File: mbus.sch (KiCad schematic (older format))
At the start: 17 parts, among them Q1 PN2222A, Q2 PN2222A, Q3 BC640, Q4 PN2222A

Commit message: some cosmetics and comments
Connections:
- net GND: now also R5.2; no longer R5.1
- net at Q3.2 (C), Q4.1 (B): now also R5.1; no longer R5.2
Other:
- note added: "L1=8/f"
- note added: "R5: 82-390 ohm"
- note added: "f=8kHz \n58% DTC\n3.3V input"
- note removed: "8kHz \n58% DTC\n3.3V input"
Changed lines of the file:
@@
 LIBS:contrib
 LIBS:valves
+LIBS:mbus-cache
 EELAYER 25 0
 EELAYER END
@@
 U 1 1 59E33253
 P 3900 4250
-F 0 "R3" V 3980 4250 50  0000 C CNN
+F 0 "R3" V 3800 4250 50  0000 C CNN
 F 1 "22k" V 3900 4250 50  0000 C CNN
 F 2 "" V 3830 4250 50  0001 C CNN
@@
 U 1 1 59E33598
 P 4350 4250
-F 0 "Q3" H 4200 4150 50  0000 L CNN
-F 1 "BC640" H 4150 4450 50  0000 L CNN
+F 0 "Q3" H 4250 4100 50  0000 L CNN
+F 1 "BC640" H 4150 4400 50  0000 L CNN
 F 2 "" H 4550 4350 50  0001 C CNN
 F 3 "" H 4350 4250 50  0001 C CNN
@@
 U 1 1 59E33697
 P 4000 4800
-F 0 "Q2" H 3850 4900 50  0000 L CNN
+F 0 "Q2" H 3900 4950 50  0000 L CNN
 F 1 "PN2222A" H 3700 4650 50  0000 L CNN
 F 2 "" H 4200 4900 50  0001 C CNN
@@
 F 3 "" H 4450 4700 50  0001 C CNN
 	1    4450 4700
-	-1   0    0    1
+	1    0    0    -1
 $EndComp
 $Comp
@@
 U 1 1 59E33F56
 P 4950 4500
-F 0 "Q4" H 4800 4600 50  0000 L CNN
-F 1 "PN2222A" H 5150 4500 50  0000 L CNN
+F 0 "Q4" H 4850 4650 50  0000 L CNN
+F 1 "PN2222A" H 4650 4350 50  0000 L CNN
 F 2 "" H 5150 4600 50  0001 C CNN
 F 3 "" H 4950 4500 50  0001 C CNN
@@
 Serial input
 Text Notes 1150 4450 0    60   ~ 0
-8kHz \n58% DTC\n3.3V input
+f=8kHz \n58% DTC\n3.3V input
+Text Notes 4600 5050 0    60   ~ 0
+R5: 82-390 ohm
+Text Notes 2100 3900 0    60   ~ 0
+L1=8/f
 $EndSCHEMATC

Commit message: transistor pinouts are different and noted on schematics
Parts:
- Q1, Q2, Q4: symbol Q_NPN_BCE -> Q_NPN_EBC
- Q3: symbol Q_PNP_BCE -> Q_PNP_ECB
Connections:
- net GND: now also Q1.1 (E), Q2.1 (E), Q4.1 (E); no longer Q1.3 (E), Q2.3 (E), Q4.3 (E)
- net MBUS-: now also Q3.1 (E); no longer Q3.3 (E)
- net TX: now also Q4.3 (C); no longer Q4.2 (C)
- net at R1.1: now also Q1.2 (B); no longer Q1.1 (B)
- net at D1.2 (A), L1.2: now also Q1.3 (C); no longer Q1.2 (C)
- net at Q3.2 (C), R5.1: now also Q4.2 (B); no longer Q4.1 (B)
- net at R2.1: now also Q2.2 (B); no longer Q2.1 (B)
- new net: Q2.3 (C), Q3.3 (B), R3.1
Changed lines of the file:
@@
 	2000 4300 1900 4300
 $Comp
-L Q_NPN_BCE Q1
+L Q_NPN_EBC Q1
 U 1 1 59E32AF3
 P 2500 4300
@@
 36V
 $Comp
-L Q_PNP_BCE Q3
+L Q_PNP_ECB Q3
 U 1 1 59E33598
 P 4350 4250
@@
 	4100 4250 4150 4250
 $Comp
-L Q_NPN_BCE Q2
+L Q_NPN_EBC Q2
 U 1 1 59E33697
 P 4000 4800
@@
 	4450 4500 4450 4550
 $Comp
-L Q_NPN_BCE Q4
+L Q_NPN_EBC Q4
 U 1 1 59E33F56
 P 4950 4500

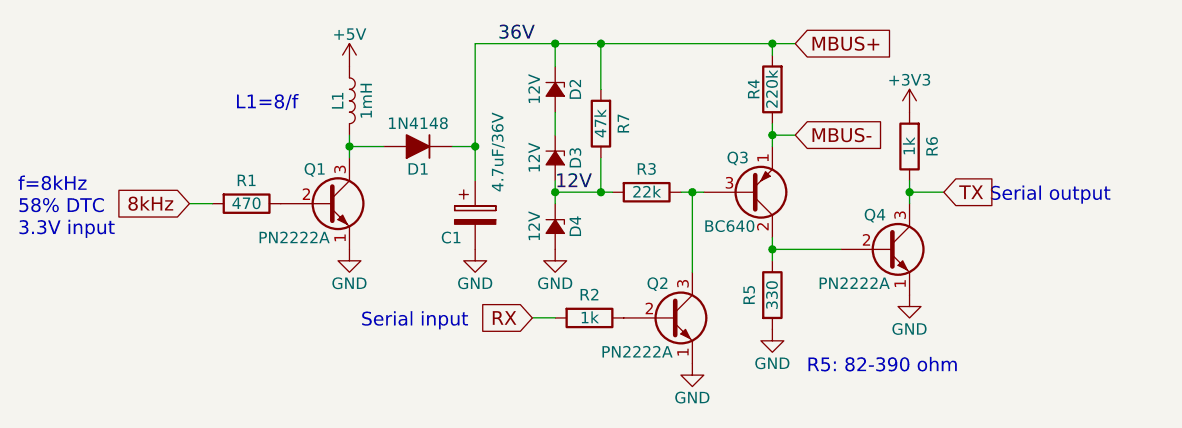
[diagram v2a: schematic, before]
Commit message: schematic cosmetic comments
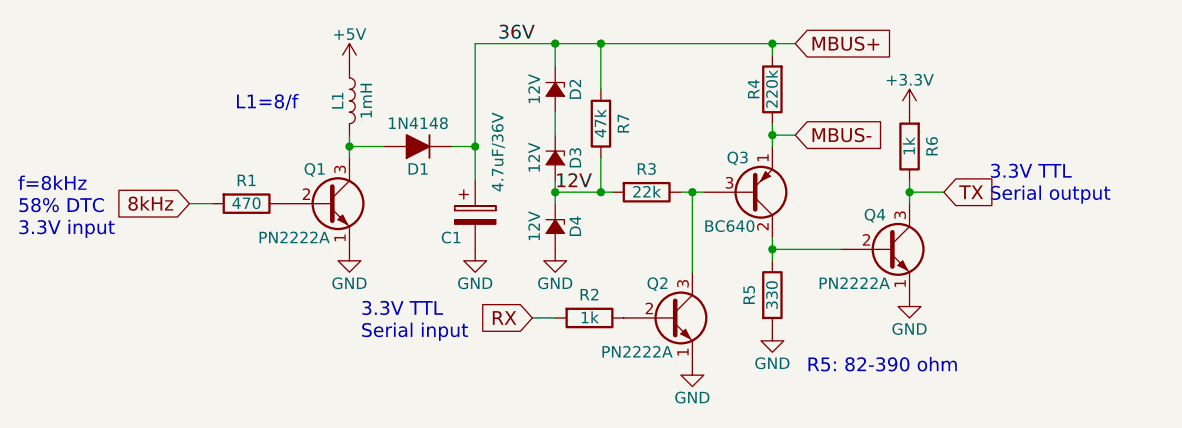
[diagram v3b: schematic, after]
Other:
- note added: "3.3V TTL\nSerial input"
- note added: "3.3V TTL\nSerial output"
- note removed: "Serial input"
- note removed: "Serial output"
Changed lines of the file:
@@
 	-1   0    0    1
-$EndComp
-$Comp
-L +3V3 #PWR7
-U 1 1 59E34677
-P 5050 3900
-F 0 "#PWR7" H 5050 3750 50  0001 C CNN
-F 1 "+3V3" H 5050 4040 50  0000 C CNN
-F 2 "" H 5050 3900 50  0001 C CNN
-F 3 "" H 5050 3900 50  0001 C CNN
-	1    5050 3900
-	1    0    0    -1
 $EndComp
 Wire Wire Line
@@
 8kHz
 Text Notes 5400 4300 0    60   ~ 0
-Serial output
-Text Notes 2650 4850 0    60   ~ 0
-Serial input
+3.3V TTL\nSerial output
+Text Notes 2650 4900 0    60   ~ 0
+3.3V TTL\nSerial input
 Text Notes 1150 4450 0    60   ~ 0
 f=8kHz \n58% DTC\n3.3V input
@@
 Text Notes 2100 3900 0    60   ~ 0
 L1=8/f
+$Comp
+L +3.3V #PWR?
+U 1 1 59E48729
+P 5050 3900
+F 0 "#PWR?" H 5050 3750 50  0001 C CNN
+F 1 "+3.3V" H 5050 4040 50  0000 C CNN
+F 2 "" H 5050 3900 50  0001 C CNN
+F 3 "" H 5050 3900 50  0001 C CNN
+	1    5050 3900
+	1    0    0    -1
+$EndComp
 $EndSCHEMATC
